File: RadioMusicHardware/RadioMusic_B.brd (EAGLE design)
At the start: 107 x 19.5 mm, 33 parts, among them IC4 TL074, U1 TEENSY_3.1_TW

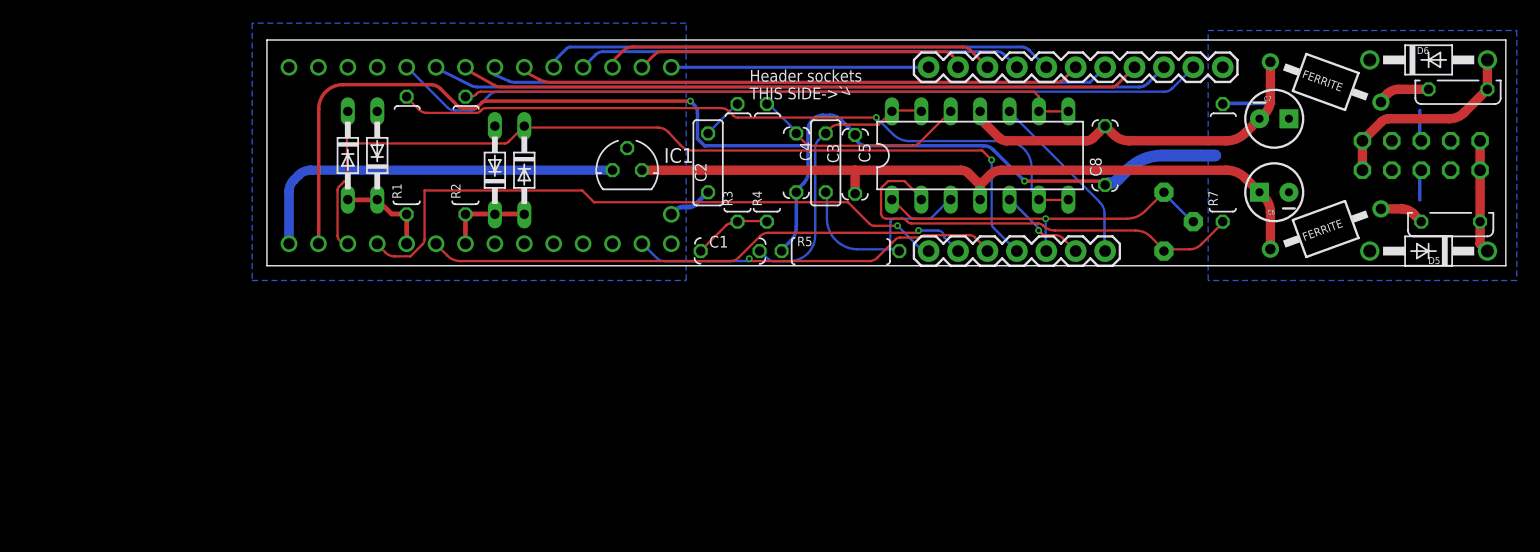
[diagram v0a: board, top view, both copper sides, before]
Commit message: WIP on a SAMD51 back board.
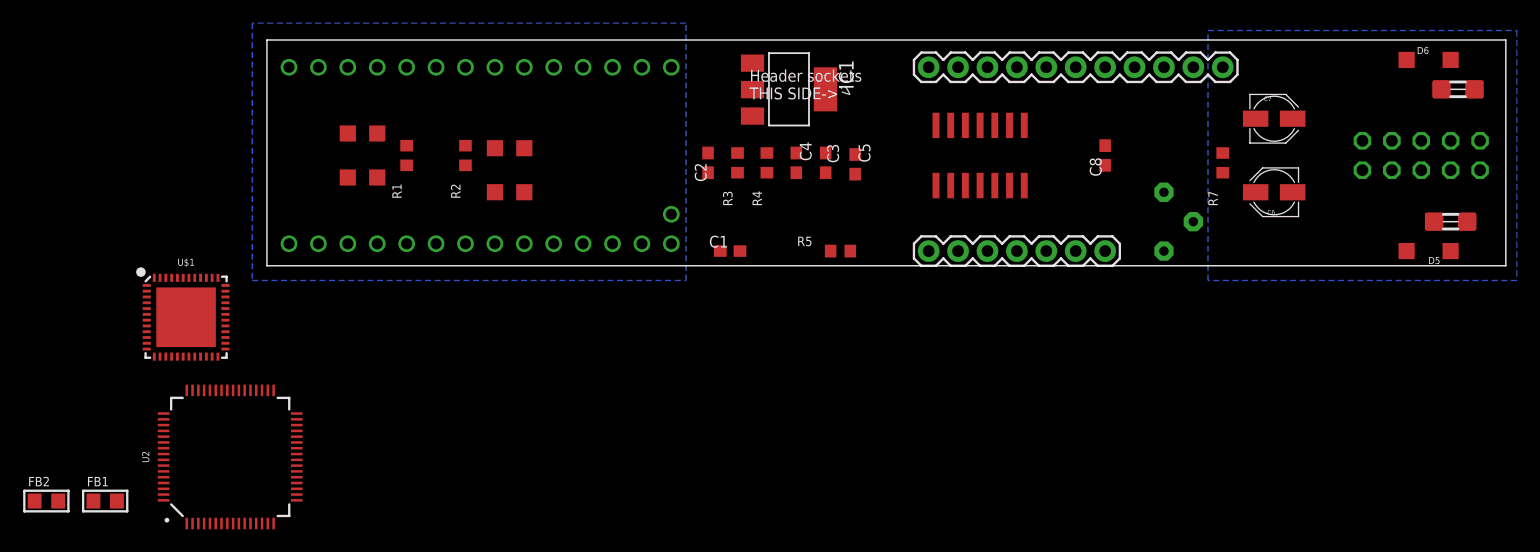
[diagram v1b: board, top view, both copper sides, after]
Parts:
- removed L1, L2: BL01RN1A, inductors:BL01RN1A
- added FB1, FB2: (no value), microbuilder:_0805
- added U$1: ATSAMD51G19A, SparkFun-IC-Microcontroller:QFN-48
- added U2: ATSAMD51J20A-A, SparkFun-IC-Microcontroller:TQFP64
- C1, C4, C5, C8: device TomW:C050-024X044 -> rcl:C0603
- C2, C3: device TomW:C050-025X075 -> rcl:C0603
- C6, C7: device SparkFun-Passives:CPOL-RADIAL-10UF-25V -> rcl:PANASONIC_B
- D1, D2, D3, D4: device diode:DO34-7 -> diode:SOD123
- D5, D6: device diode:DO41-10 -> diode:SOD123
- F1, F2: device TomW:C050H075X075 -> _JC:F1206
- IC1: value (none) -> REG1117; device v-reg:78LXX -> burr-brown:SOT223
- IC4: device linear:DIL14 -> Foxfield:SO14
- R1, R2, R3, R4, R5, R7: device TomW:0207/10 -> rcl:R0603
- moved IC1 15.6 mm to (45.1, 15.2), turned to 270 degrees
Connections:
- removed net +5V: IC1.OUT, U1.VIN
- new net 3V3: IC1.2, U1.VIN
- net +12V: now also C6.+, FB1.2, IC1.3; no longer C6.1, IC1.IN, L1.1
- net -12V: now also C7.-, FB2.2; no longer C7.2, L2.1
- net DGND: now also IC1.1; no longer IC1.GND
- net GND: now also C6.-, C7.+; no longer C6.2, C7.1
- net N$22: now also FB1.1; no longer L1.2
- net N$23: now also FB2.1; no longer L2.2
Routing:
- net GND: track 118.8 -> 0.00 mm, vias 2 -> 0
- net +3.3V: track 78.3 -> 0.00 mm, vias 1 -> 0
- net LED1: track 70.8 -> 0.00 mm
- net LED2: track 63.9 -> 0.00 mm
- net +12V: track 63.4 -> 0.00 mm
- net N$3: track 62.1 -> 0.00 mm, vias 1 -> 0
- net LED3: track 59.0 -> 0.00 mm
- net CHANNEL_POT: track 55.1 -> 0.00 mm, vias 1 -> 0
- net LED4: track 54.0 -> 0.00 mm
- net N$1: track 53.6 -> 0.00 mm
- net MOSI: track 48.7 -> 0.00 mm
- net TIME_POT: track 47.3 -> 0.00 mm, vias 1 -> 0
- net RESET_SW: track 44.2 -> 0.00 mm
- net RESET_CV: track 38.5 -> 0.00 mm
- net N$7: track 38.2 -> 0.00 mm
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
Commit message: Rear Board for SAMD51.
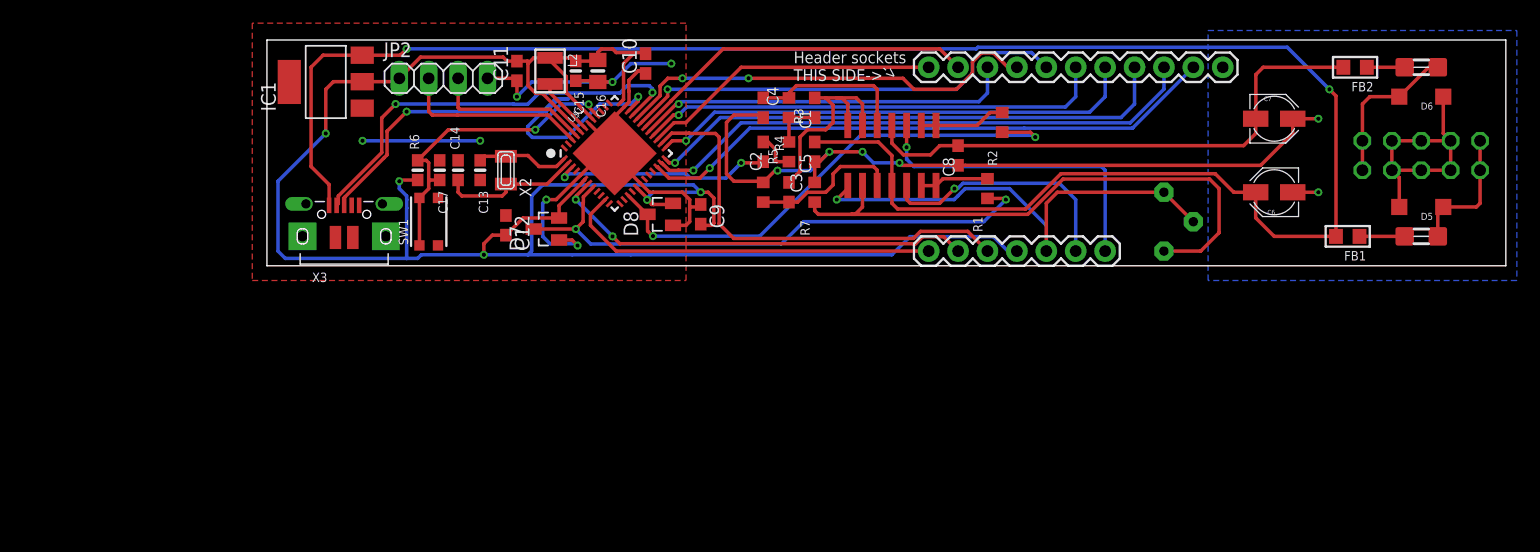
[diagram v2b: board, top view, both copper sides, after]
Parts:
- removed D1, D2, D3, D4: BAT42, diode:SOD123
- removed U1: TEENSY_3.1_TW, TomW:TEENSY_3.1_TW
- removed U2: ATSAMD51J20A-A, SparkFun-IC-Microcontroller:TQFP64
- added C10, C11, C12, C9: 100n, adafruit:C0603
- added C13, C14: 22pF, microbuilder:0603-NO
- added C15: 1u, microbuilder:0603-NO
- added C16: 10uF, microbuilder:0805-NO
- added C17: 1uF, microbuilder:0603-NO
- added D7, D8: BAT54S, diode:SOT23
- added JP2: (no value), pinhead:1X04
- added L2: 10uH, microbuilder:INDUCTOR_1007
- added R6: 10K, microbuilder:0603-NO
- added SW1: KMR2, microbuilder:BTN_KMR2_4.6X2.8
- added X2: 32.768, adafruit2:XTAL3215
- added X3: microUSB, microbuilder:4UCONN_20329_V2
- moved FB2 119.1 mm to (94.0, 17.1), turned to 180 degrees
- moved FB1 109.7 mm to (93.3, 2.54), turned to 180 degrees
- moved R1 50.2 mm to (62.2, 6.67)
- moved R2 46.4 mm to (63.5, 12.4)
- moved IC1 40.0 mm to (5.08, 15.9), turned to 90 degrees
- moved U$1 39.6 mm to (30.0, 9.71), turned to 45 degrees
- moved R7 35.3 mm to (47.3, 6.35)
- moved C1 14.4 mm to (47.3, 13.7), turned to 90 degrees
- moved C8 12.7 mm to (59.7, 9.53)
- moved R5 8.38 mm to (42.9, 6.35), turned to 270 degrees
- moved IC4 7.62 mm to (54.0, 9.53)
- moved C4 5.55 mm to (42.9, 13.7)
- moved R4 5.13 mm to (45.1, 13.7)
- moved C2 4.86 mm to (42.9, 9.84)
- moved R3 4.55 mm to (45.1, 9.84), turned to 270 degrees
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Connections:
- removed net +3.3V: D1.C, D3.C, JP3.4, U1.3.3V
- new net !RESET: C17.2, R6.2, SW1.A, SW1.A', U$1.40
- new net D+: U$1.34, X3.D+
- new net D-: U$1.33, X3.D-
- new net N$11: L2.P$2, U$1.43
- new net N$13: U$1.39
- new net N$8: C13.1, U$1.1, X2.P$1
- new net N$9: C14.1, U$1.2, X2.P$2
- new net SWCLK: JP2.3, U$1.45
- new net SWDIO: JP2.2, U$1.46
- net +12V: now also X3.VBUS
- net 3V3: now also C10.2, C11.2, C12.2, C15.1, C16.1, C9.2, D7.2, D8.2, JP2.1, JP3.4, L2.P$1, R6.1, U$1.17, U$1.36, U$1.41, U$1.44, U$1.6; no longer U1.VIN
- net CHANNEL_POT: now also U$1.11; no longer U1.23/A9
- net DAC: now also U$1.3; no longer U1.DAC
- net DGND: now also C10.1, C11.1, C12.1, C13.2, C14.2, C15.2, C16.2, C17.1, C9.1, D7.1, D8.1, JP2.4, SW1.B, SW1.B', U$1.18, U$1.35, U$1.42, U$1.5, U$1.EP, X3.BASE@1, X3.BASE@2, X3.GND, X3.SPRT@1, X3.SPRT@2, X3.SPRT@3, X3.SPRT@4; no longer D2.A, D4.A, U1.GND
- net GND: no longer U1.AGND
- net LED1: now also U$1.22; no longer U1.3
- net LED2: now also U$1.23; no longer U1.4
- net LED3: now also U$1.24; no longer U1.5
- net LED4: now also U$1.25; no longer U1.6
- net LED_RESET: now also U$1.30; no longer U1.11
- net MISO: now also U$1.27; no longer U1.12
- net MOSI: now also U$1.28; no longer U1.7
- net PIN20/A6: now also D8.3, U$1.15; no longer D3.A, D4.C, U1.20/A6
- net PIN22/A8: now also D7.3, U$1.8; no longer D1.A, D2.C, U1.22/A8
- net RESET_CV: now also U$1.32; no longer U1.9
- net RESET_SW: now also U$1.31; no longer U1.8
- net SCLK: now also U$1.26; no longer U1.14/A0
- net SS: now also U$1.29; no longer U1.10
- net TIME_POT: now also U$1.7; no longer U1.21/A7
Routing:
- net 3V3: track 0.00 -> 187.4 mm, vias 0 -> 5
- net +12V: track 0.00 -> 170.3 mm, vias 0 -> 2
- net GND: track 0.00 -> 91.9 mm, vias 0 -> 6
- net DGND: track 0.00 -> 63.1 mm, vias 0 -> 7
- net LED1: track 0.00 -> 50.7 mm, vias 0 -> 1
- net N$7: track 0.00 -> 49.7 mm
- net PIN22/A8: track 0.00 -> 48.8 mm, vias 0 -> 2
- net LED2: track 0.00 -> 48.6 mm, vias 0 -> 1
- net -12V: track 0.00 -> 47.1 mm
- net LED3: track 0.00 -> 46.0 mm, vias 0 -> 1
- net PIN20/A6: track 0.00 -> 44.2 mm, vias 0 -> 2
- net D+: track 0.00 -> 42.6 mm, vias 0 -> 2
- net LED4: track 0.00 -> 42.4 mm, vias 0 -> 1
- net AUDIO_OUT: track 0.00 -> 41.9 mm, vias 0 -> 1
- net MOSI: track 0.00 -> 40.5 mm, vias 0 -> 1
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- added copper zone on layer 1, net DGND
- removed copper zone on layer 16, net DGND
